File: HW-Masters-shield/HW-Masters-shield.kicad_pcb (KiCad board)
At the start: 2 copper layers, 78.3 x 80.9 mm, 57 parts, among them J1 12V, J2 Bornera 2, J3 Salida de relevador, J4 Bornera 1, K1 G5LE-1, Q1 ntr4003nt1g

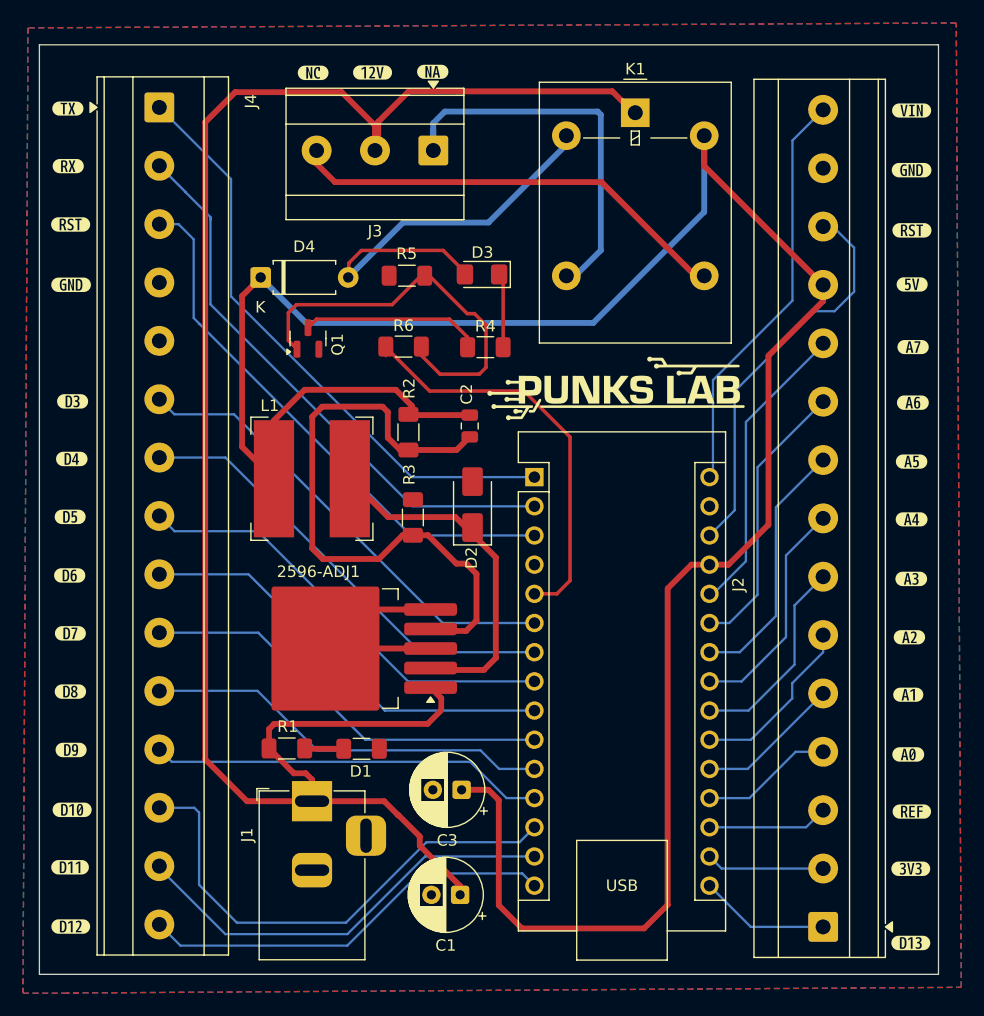
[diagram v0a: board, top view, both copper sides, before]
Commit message: FEAT: crrijo error de mosfet y de falta de berreno de montaje
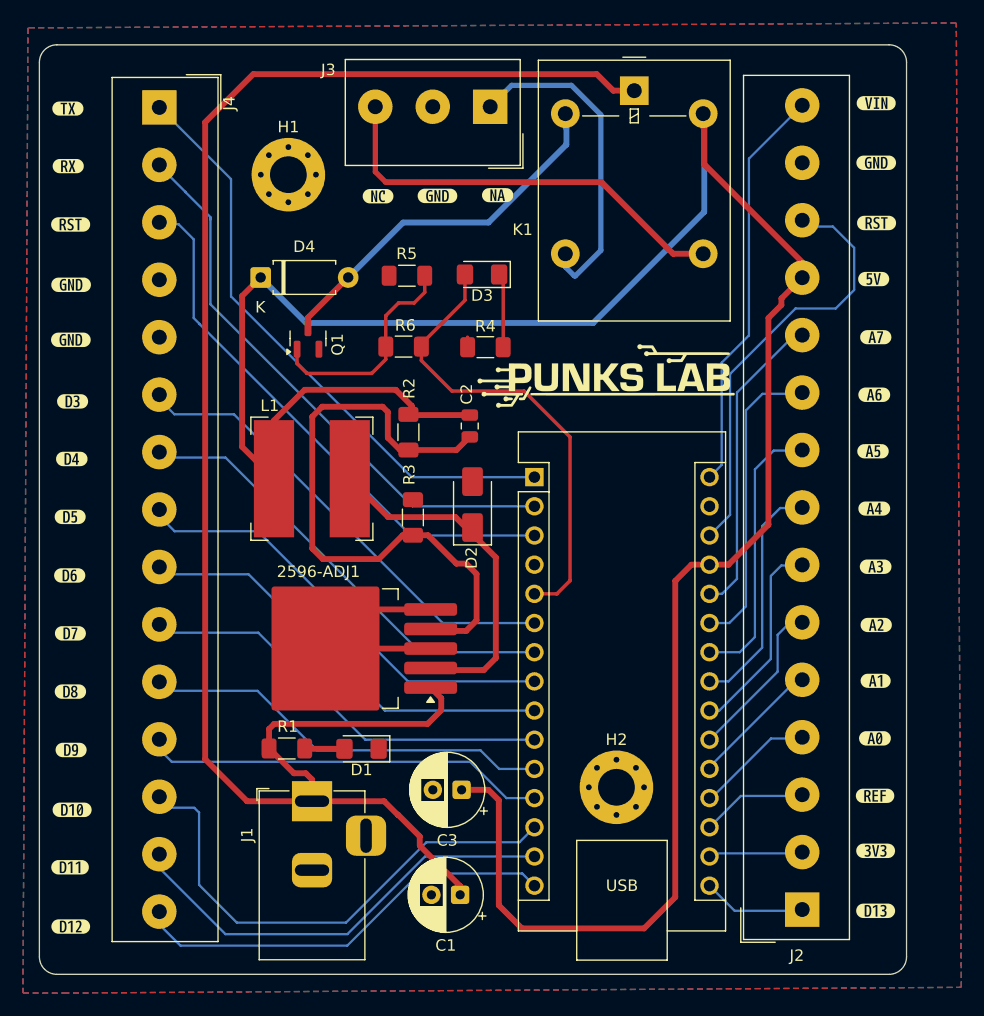
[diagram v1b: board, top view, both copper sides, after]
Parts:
- removed kibuzzard-69E52924: G***, kibuzzard-69E52924
- added H1: MountingHole, MountingHole:MountingHole_3.2mm_M3_Pad_Via, F.Cu at (95.5, 61.4)
- added H2: MountingHole, MountingHole:MountingHole_3.2mm_M3_Pad_Via, F.Cu at (124.0, 114.7)
- added kibuzzard-69E529CF: G***, kibuzzard-69E529CF, F.Cu at (76.5, 75.8)
- added kibuzzard-6A12559C: G***, kibuzzard-6A12559C, F.Cu at (108.5, 63.2)
- D1: footprint Resistor_SMD:R_1206_3216Metric_Pad1.30x1.75mm_HandSolder -> Diode_SMD:D_1206_3216Metric_Pad1.42x1.75mm_HandSolder
- D3: footprint LED_SMD:LED_1206_3216Metric_Pad1.42x1.75mm_HandSolder -> Diode_SMD:D_1206_3216Metric_Pad1.42x1.75mm_HandSolder
- J2, J4: footprint TerminalBlock_Phoenix:TerminalBlock_Phoenix_MKDS-3-15-5.08_1x15_P5.08mm_Horizontal -> TerminalBlock_Altech:Altech_AK100_1x15_P5.00mm
- J3: footprint TerminalBlock_Phoenix:TerminalBlock_Phoenix_MKDS-3-3-5.08_1x03_P5.08mm_Horizontal -> TerminalBlock_Altech:Altech_AK100_1x03_P5.00mm
- Q1: value ntr4003nt1g -> ntr4003nt1g O AO 3400
- R4: value 1k -> 330
- moved G*** 27.0 mm to (103.7, 101.8), turned to -90 degrees
- moved G*** 16.9 mm to (124.6, 95.6)
- moved kibuzzard-69E52917 12.1 mm to (103.3, 63.3)
- moved kibuzzard-69E52931 12.1 mm to (113.7, 63.2)
- moved J3 6.25 mm to (113.0, 55.5)
- moved kibuzzard-69E52B68 4.15 mm to (146.6, 125.5)
- moved kibuzzard-69E52BB2 3.48 mm to (146.6, 115.5)
- moved kibuzzard-69E52C0F 3.48 mm to (146.4, 85.5)
- moved kibuzzard-69E52B9F 3.43 mm to (146.6, 120.2)
- moved kibuzzard-69E52C29 3.43 mm to (146.5, 80.5)
- moved kibuzzard-69E52C1C 3.38 mm to (146.5, 90.5)
- moved kibuzzard-69E52C44 3.38 mm to (146.4, 70.5)
- moved kibuzzard-69E52C38 3.36 mm to (146.6, 75.5)
- moved kibuzzard-69E52C05 3.28 mm to (146.6, 95.5)
- moved kibuzzard-69E52BC8 3.22 mm to (146.5, 110.5)
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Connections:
- D3 pad 2: Net-(D3-A) -> /PIN_{5}
- D4 pad 2: Net-(D3-A) -> Net-(D4-A)
- J3 pad 2: +12V -> GND
- J4 pad 5: unconnected-(J4-Pin_5-Pad5) -> GND
- K1 pad 2: Net-(D3-A) -> Net-(D4-A)
- Q1 pad 3: Net-(Q1-D) -> Net-(D4-A)
- R4 pad 1: Net-(Q1-D) -> GND
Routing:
- net Net-(D3-A): track 37.4 -> 0.00 mm
- net Net-(D4-A): track 0.00 -> 32.4 mm
- net Net-(Q1-D): track 15.7 -> 0.00 mm
- net Net-(Q1-G): track 34.8 -> 20.7 mm
- net +12V: track 156.3 -> 149.6 mm
- net Net-(J3-Pin_1): track 35.1 -> 28.7 mm
- net +5V: track 203.5 -> 208.1 mm
- net /PIN_{5}: track 36.3 -> 40.5 mm
- net /PIN_{28}: track 34.7 -> 37.8 mm
- net /PIN_{17}: track 10.3 -> 8.23 mm
- net /PIN_{25}: track 24.4 -> 26.4 mm
- net Net-(J3-Pin_3): track 39.0 -> 37.2 mm
- net /PIN_{16}: track 11.4 -> 9.70 mm
- net /PIN_{24}: track 22.4 -> 23.9 mm
- net /PIN_{19}: track 11.6 -> 10.3 mm
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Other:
- board size 78.3 x 80.9 mm -> 75.5 x 80.9 mm
